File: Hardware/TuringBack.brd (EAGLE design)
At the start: 107 x 49.5 mm, 45 parts, among them IC11 78L09, IC12 78L09, IC7 TL072P

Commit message: Rev 4 Front and Back Boards complete
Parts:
- renumbered BACK_BUS2 to LINK1, BACK_PWR to LINK2, BUS_1_BACK to LINK3
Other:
- board text added: ">>RED>>"
- board text added: "EXPANDER OUTPUTS ONLY"
- board text added: "Music Thing Modular Turing Machine Rev4 Back Board Designed in Herne Hill, London By Tom Whitwell January 2016 CC-BY-SA musicthing.co.uk"
- board text removed: "Music Thing Modular Turing Machine Rev4 Prototype 1 Back Board Designed in Herne Hill, London By Tom Whitwell September 2015 CC-BY-SA"

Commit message: Finalised V4 PCBs
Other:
- board text added: "Allen Strange"
- board text added: "Cage"
- board text added: "Dieter Doepfer"
- board text added: "Don Buchla"
- board text added: "Fredkin & Minsky"
- board text added: "Grant Richter"
- board text added: "Hal Chamberlin"
- board text added: "Inspired by:"
- board text added: "John"
- board text added: "K.F.W"
- board text added: "Ken Stone"
- board text added: "Lunetta"
- board text added: "Navs"
- board text added: "Nicholas Collins"
- board text added: "Philip Glass"
- board text added: "Stanley"
- board text added: "Steve Reich"
- board text added: "Steven Grimley-Taylor"
- board text added: "Terry Riley"
- board text added: "The Muff Wigglers"
- board text added: "Tony Steventon"
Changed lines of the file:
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@@
 <layer number="14" name="Route14" color="1" fill="6" visible="no" active="no"/>
 <layer number="15" name="Route15" color="4" fill="6" visible="no" active="yes"/>
-<layer number="16" name="Bottom" color="1" fill="1" visible="no" active="yes"/>
+<layer number="16" name="Bottom" color="1" fill="1" visible="yes" active="yes"/>
 <layer number="17" name="Pads" color="10" fill="1" visible="yes" active="yes"/>
 <layer number="18" name="Vias" color="2" fill="1" visible="yes" active="yes"/>
-<layer number="19" name="Unrouted" color="6" fill="1" visible="no" active="yes"/>
+<layer number="19" name="Unrouted" color="6" fill="1" visible="yes" active="yes"/>
 <layer number="20" name="Dimension" color="15" fill="1" visible="yes" active="yes"/>
-<layer number="21" name="tPlace" color="7" fill="1" visible="yes" active="yes"/>
-<layer number="22" name="bPlace" color="7" fill="1" visible="no" active="yes"/>
-<layer number="23" name="tOrigins" color="15" fill="1" visible="yes" active="yes"/>
-<layer number="24" name="bOrigins" color="15" fill="1" visible="no" active="yes"/>
-<layer number="25" name="tNames" color="7" fill="1" visible="yes" active="yes"/>
+<layer number="21" name="tPlace" color="7" fill="1" visible="no" active="yes"/>
+<layer number="22" name="bPlace" color="7" fill="1" visible="yes" active="yes"/>
+<layer number="23" name="tOrigins" color="15" fill="1" visible="no" active="yes"/>
+<layer number="24" name="bOrigins" color="15" fill="1" visible="yes" active="yes"/>
+<layer number="25" name="tNames" color="7" fill="1" visible="no" active="yes"/>
 <layer number="26" name="bNames" color="7" fill="1" visible="no" active="yes"/>
-<layer number="27" name="tValues" color="7" fill="1" visible="yes" active="yes"/>
+<layer number="27" name="tValues" color="7" fill="1" visible="no" active="yes"/>
 <layer number="28" name="bValues" color="7" fill="1" visible="no" active="yes"/>
 <layer number="29" name="tStop" color="7" fill="3" visible="no" active="yes"/>
-<layer number="30" name="bStop" color="7" fill="6" visible="no" active="yes"/>
+<layer number="30" name="bStop" color="7" fill="6" visible="yes" active="yes"/>
 <layer number="31" name="tCream" color="7" fill="4" visible="no" active="yes"/>
 <layer number="32" name="bCream" color="7" fill="5" visible="no" active="yes"/>
@@
 <layer number="40" name="bKeepout" color="1" fill="11" visible="no" active="yes"/>
 <layer number="41" name="tRestrict" color="4" fill="10" visible="no" active="yes"/>
-<layer number="42" name="bRestrict" color="1" fill="10" visible="no" active="yes"/>
+<layer number="42" name="bRestrict" color="1" fill="10" visible="yes" active="yes"/>
 <layer number="43" name="vRestrict" color="2" fill="10" visible="no" active="yes"/>
 <layer number="44" name="Drills" color="7" fill="1" visible="no" active="yes"/>
@@
 <wire x1="107" y1="49.5" x2="0" y2="49.5" width="0" layer="20"/>
 <wire x1="-15.875" y1="24.75" x2="121.285" y2="24.75" width="0.05" layer="51"/>
-<text x="98.425" y="1.27" size="1.016" layer="22" font="vector" rot="SMR90">Music Thing Modular Turing Machine
+<text x="84.455" y="27.305" size="1.016" layer="22" font="vector" rot="SMR0">Music Thing Modular Turing Machine
 Rev4  Back Board
 Designed in Herne Hill, London By Tom Whitwell
@@
 </polygon>
 <text x="84.455" y="13.97" size="2.286" layer="22" rot="MR0">EXPANDER OUTPUTS ONLY</text>
+<text x="104.127234375" y="27.377475" size="1.016" layer="30" ratio="12" rot="MR90">Don Buchla</text>
+<text x="98.627628125" y="31.972203125" size="1.016" layer="30" ratio="12" rot="MR90">Ken Stone</text>
+<text x="100.630615625" y="27.0115" size="1.016" layer="30" ratio="12" rot="MR90">Grant Richter</text>
+<text x="105.605978125" y="18.229196875" size="1.016" layer="30" ratio="12" rot="MR90">Hal Chamberlin</text>
+<text x="102.2196125" y="21.173090625" size="1.016" layer="30" ratio="12" rot="MR90">Allen Strange</text>
+<text x="94.02604375" y="33.508940625" size="1.016" layer="30" ratio="12" rot="MR90">Fredkin &amp; Minsky</text>
+<text x="96.389121875" y="35.142478125" size="1.016" layer="30" ratio="12" rot="MR90">Nicholas Collins</text>
+<text x="98.4197375" y="10.113390625" size="1.016" layer="30" ratio="12" rot="MR90">Navs</text>
+<text x="90.79385" y="42.12758125" size="1.016" layer="30" ratio="12" rot="MR90">Lunetta</text>
+<text x="99.34384375" y="15.06238125" size="1.016" layer="30" ratio="12" rot="MR90">Dieter Doepfer</text>
+<text x="105.269009375" y="36.180021875" size="1.016" layer="30" ratio="12" rot="MR90">Philip Glass</text>
+<text x="103.112259375" y="38.498478125" size="1.016" layer="30" ratio="12" rot="MR90">Steve Reich</text>
+<text x="103.34131875" y="1.8847875" size="1.016" layer="30" ratio="12" rot="MR90">Steven Grimley-Taylor</text>
+<text x="92.112265625" y="39.271515625" size="1.016" layer="30" ratio="12" rot="MR90">Stanley</text>
+<text x="101.038353125" y="5.615478125" size="1.016" layer="30" ratio="12" rot="MR90">The Muff Wigglers</text>
+<text x="96.4004875" y="14.234275" size="1.016" layer="30" ratio="12" rot="MR90">K.F.W</text>
+<text x="101.271" y="39.003278125" size="1.016" layer="30" ratio="12" rot="MR90">John</text>
+<text x="100.1762625" y="39.752578125" size="1.016" layer="30" ratio="12" rot="MR90">Cage</text>
+<text x="99.302259375" y="44.213478125" size="1.016" layer="30" ratio="12" rot="MR90">Terry
+Riley</text>
+<text x="105.605978125" y="2.354196875" size="1.016" layer="30" ratio="12" rot="MR90">Inspired by:</text>
+<text x="94.4954875" y="9.154275" size="1.016" layer="30" ratio="12" rot="MR90">Tony
+Steventon</text>
 </plain>
 <attributes>

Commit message: Silkscreen change on Back Board
Added + - symbols to fuses in power supply
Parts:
- +FUSE: value FUSE -> +FUSE
- -FUSE: value FUSE -> -FUSE
- renumbered F1 to +FUSE, F2 to -FUSE
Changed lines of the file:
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@@
 <layer number="19" name="Unrouted" color="6" fill="1" visible="yes" active="yes"/>
 <layer number="20" name="Dimension" color="15" fill="1" visible="yes" active="yes"/>
-<layer number="21" name="tPlace" color="7" fill="1" visible="no" active="yes"/>
-<layer number="22" name="bPlace" color="7" fill="1" visible="yes" active="yes"/>
-<layer number="23" name="tOrigins" color="15" fill="1" visible="no" active="yes"/>
-<layer number="24" name="bOrigins" color="15" fill="1" visible="yes" active="yes"/>
-<layer number="25" name="tNames" color="7" fill="1" visible="no" active="yes"/>
+<layer number="21" name="tPlace" color="7" fill="1" visible="yes" active="yes"/>
+<layer number="22" name="bPlace" color="7" fill="1" visible="no" active="yes"/>
+<layer number="23" name="tOrigins" color="15" fill="1" visible="yes" active="yes"/>
+<layer number="24" name="bOrigins" color="15" fill="1" visible="no" active="yes"/>
+<layer number="25" name="tNames" color="7" fill="1" visible="yes" active="yes"/>
 <layer number="26" name="bNames" color="7" fill="1" visible="no" active="yes"/>
-<layer number="27" name="tValues" color="7" fill="1" visible="no" active="yes"/>
+<layer number="27" name="tValues" color="7" fill="1" visible="yes" active="yes"/>
 <layer number="28" name="bValues" color="7" fill="1" visible="no" active="yes"/>
 <layer number="29" name="tStop" color="7" fill="3" visible="no" active="yes"/>
@@
 <attribute name="VALUE" x="12.192" y="1.524" size="1.016" layer="27" ratio="10" rot="R180"/>
 </element>
-<element name="F1" library="TomW" package="C050H075X075" value="FUSE" x="6.35" y="15.875" smashed="yes">
-<attribute name="VALUE" x="5.08" y="15.875" size="0.889" layer="27" ratio="10"/>
+<element name="+FUSE" library="TomW" package="C050H075X075" value="+FUSE" x="6.35" y="15.875" smashed="yes">
+<attribute name="VALUE" x="4.445" y="15.875" size="0.889" layer="27" ratio="10"/>
 </element>
-<element name="F2" library="TomW" package="C050H075X075" value="FUSE" x="6.35" y="5.715" smashed="yes">
-<attribute name="VALUE" x="5.08" y="5.715" size="0.889" layer="27" ratio="10"/>
+<element name="-FUSE" library="TomW" package="C050H075X075" value="-FUSE" x="6.35" y="5.715" smashed="yes">
+<attribute name="VALUE" x="4.572" y="5.715" size="0.889" layer="27" ratio="10"/>
 </element>
 <element name="L1" library="inductors" package="BL01RN1A" value="BL01RN1A" x="17.78" y="17.78" smashed="yes" rot="R20"/>
@@
 <contactref element="SV1" pad="10"/>
 <contactref element="SV1" pad="9"/>
-<contactref element="F1" pad="1"/>
+<contactref element="+FUSE" pad="1"/>
 <contactref element="D5" pad="C"/>
 <wire x1="13.97" y1="9.525" x2="13.97" y2="12.065" width="0.8128" layer="1"/>
@@
 <contactref element="SV1" pad="1"/>
 <contactref element="SV1" pad="2"/>
-<contactref element="F2" pad="1"/>
+<contactref element="-FUSE" pad="1"/>
 <contactref element="D6" pad="A"/>
 <wire x1="3.81" y1="12.065" x2="3.81" y2="9.525" width="0.8128" layer="1"/>
@@
 <signal name="N$42" class="1">
 <contactref element="L1" pad="1"/>
-<contactref element="F1" pad="2"/>
+<contactref element="+FUSE" pad="2"/>
 <wire x1="8.89" y1="15.875" x2="12.838821875" y2="15.875" width="0.8128" layer="1"/>
 <wire x1="12.838821875" y1="15.875" x2="13.006359375" y2="16.0425375" width="0.8128" layer="1"/>
 </signal>
 <signal name="N$44" class="1">
-<contactref element="F2" pad="2"/>
+<contactref element="-FUSE" pad="2"/>
 <contactref element="L2" pad="1"/>
 <wire x1="8.89" y1="5.715" x2="12.5389" y2="5.715" width="0.8128" layer="1"/>

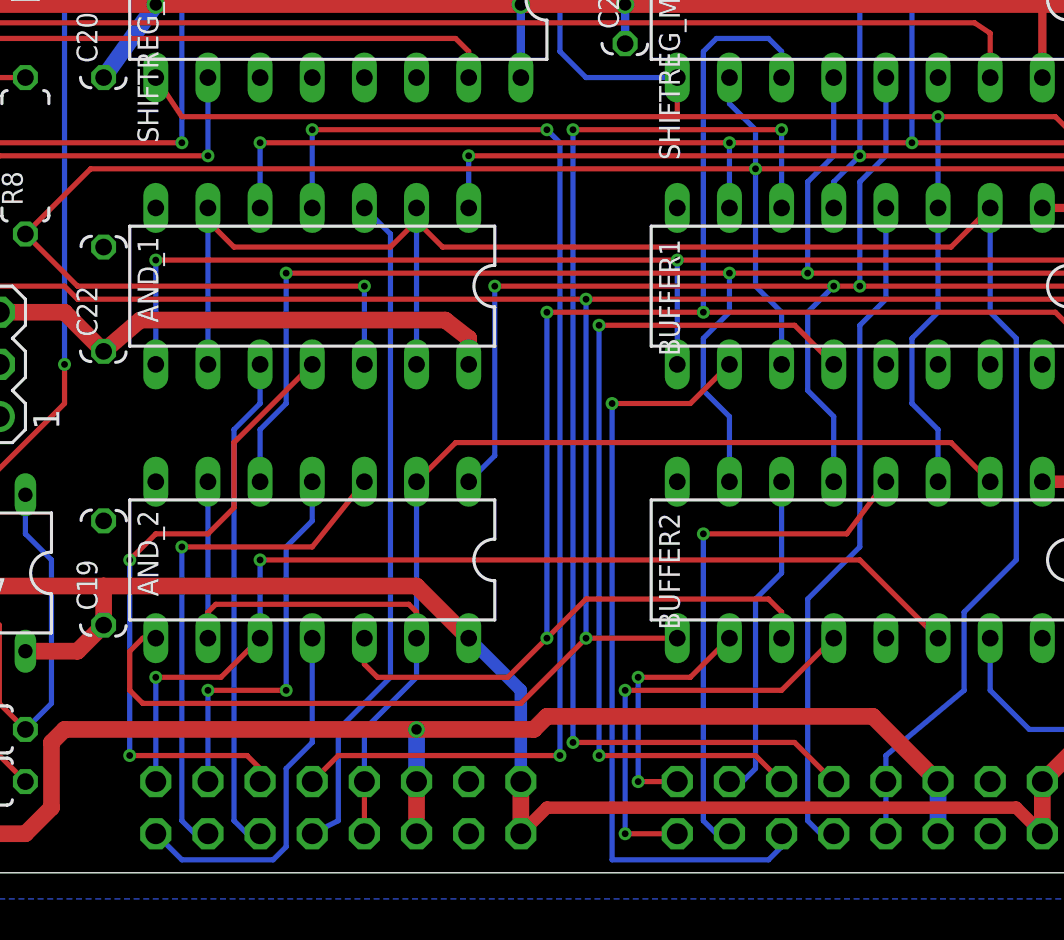
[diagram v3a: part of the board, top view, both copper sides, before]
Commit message: Schematic fixed, back board needs to be routed
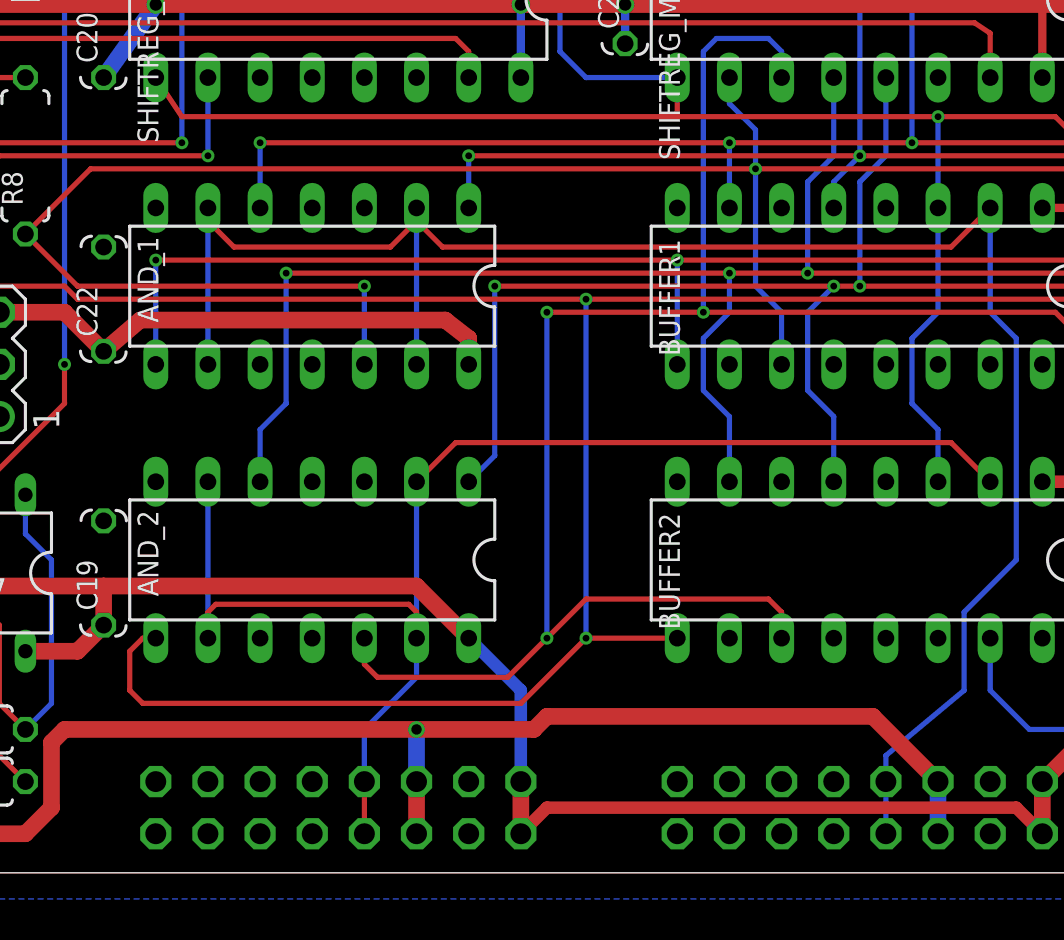
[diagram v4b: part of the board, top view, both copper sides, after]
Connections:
- net GATE1: now also BUFFER1.4; no longer BUFFER2.10
- net GATE2: now also BUFFER1.6; no longer BUFFER2.12
- net GATE3: now also BUFFER1.10; no longer BUFFER2.6
- net GATE4: now also BUFFER1.12; no longer BUFFER2.4
- net GATE5: now also BUFFER2.4; no longer BUFFER1.12
- net GATE6: now also BUFFER2.6; no longer BUFFER1.10
- net GATE7: now also BUFFER2.12; no longer BUFFER1.6
- net GATE8: now also BUFFER2.10; no longer BUFFER1.4
- net PULSE1: now also AND_1.3; no longer AND_2.10
- net PULSE2: now also AND_1.4; no longer AND_2.11
- net PULSE3: now also AND_1.10; no longer AND_2.4
- net PULSE4: now also AND_1.11; no longer AND_2.3
- net PULSE5: now also AND_2.3; no longer AND_1.11
- net PULSE6: now also AND_2.4; no longer AND_1.10
- net PULSE7: now also AND_2.11; no longer AND_1.4
- net PULSE8: now also AND_2.10; no longer AND_1.3
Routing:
- net PULSE7: track 58.6 -> 0.00 mm, vias 3 -> 0
- net GATE7: track 57.3 -> 0.00 mm, vias 3 -> 0
- net PULSE1: track 49.4 -> 0.00 mm, vias 2 -> 0
- net GATE5: track 42.6 -> 0.00 mm, vias 2 -> 0
- net GATE6: track 37.9 -> 0.00 mm, vias 1 -> 0
- net GATE8: track 33.0 -> 0.00 mm
- net PULSE8: track 32.8 -> 0.00 mm
- net PULSE5: track 31.5 -> 0.00 mm, vias 2 -> 0
- net GATE4: track 25.7 -> 0.00 mm, vias 1 -> 0
- net PULSE4: track 25.3 -> 0.00 mm, vias 1 -> 0
- net PULSE6: track 24.3 -> 0.00 mm
- net GATE2: track 20.7 -> 0.00 mm, vias 2 -> 0
- net PULSE3: track 18.9 -> 0.00 mm, vias 2 -> 0
- net PULSE2: track 17.8 -> 0.00 mm
- net GATE3: track 16.0 -> 0.00 mm
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
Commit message: routing started
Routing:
- net GATE2: track 0.00 -> 48.6 mm, vias 0 -> 2
- net GATE1: track 0.00 -> 40.9 mm, vias 0 -> 2
- net GATE4: track 0.00 -> 26.0 mm
- net GATE3: track 0.00 -> 21.4 mm
- net GATE6: track 0.00 -> 18.2 mm, vias 0 -> 1
- net GATE8: track 0.00 -> 17.8 mm
- net GATE7: track 0.00 -> 6.98 mm
- net -12V_BACK: track 105.0 -> 104.3 mm
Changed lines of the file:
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@@
 <contactref element="GATES" pad="1"/>
 <contactref element="BUFFER1" pad="4"/>
-<wire x1="67.31" y1="4.445" x2="77.47" y2="32.385" width="0" layer="19" extent="1-1"/>
+<wire x1="77.47" y1="32.385" x2="77.47" y2="27.94" width="0.254" layer="16"/>
+<wire x1="77.47" y1="27.94" x2="76.2" y2="26.67" width="0.254" layer="16"/>
+<wire x1="76.2" y1="26.67" x2="64.77" y2="26.67" width="0.254" layer="1"/>
+<wire x1="64.77" y1="26.67" x2="64.77" y2="6.985" width="0.254" layer="16"/>
+<wire x1="64.77" y1="6.985" x2="67.31" y2="4.445" width="0.254" layer="16"/>
+<via x="76.2" y="26.67" extent="1-16" drill="0.3302"/>
+<via x="64.77" y="26.67" extent="1-16" drill="0.3302"/>
 </signal>
 <signal name="GATE2">
 <contactref element="GATES" pad="2"/>
 <contactref element="BUFFER1" pad="6"/>
-<wire x1="67.31" y1="1.905" x2="72.39" y2="32.385" width="0" layer="19" extent="1-1"/>
+<wire x1="72.39" y1="32.385" x2="72.39" y2="36.195" width="0.254" layer="16"/>
+<wire x1="72.39" y1="36.195" x2="63.5" y2="36.195" width="0.254" layer="1"/>
+<wire x1="63.5" y1="36.195" x2="63.5" y2="5.715" width="0.254" layer="16"/>
+<wire x1="63.5" y1="5.715" x2="67.31" y2="1.905" width="0.254" layer="16"/>
+<via x="72.39" y="36.195" extent="1-16" drill="0.3302"/>
+<via x="63.5" y="36.195" extent="1-16" drill="0.3302"/>
 </signal>
 <signal name="GATE3">
 <contactref element="GATES" pad="3"/>
 <contactref element="BUFFER1" pad="10"/>
-<wire x1="69.85" y1="4.445" x2="69.85" y2="24.765" width="0" layer="19" extent="1-1"/>
+<wire x1="69.85" y1="24.765" x2="69.85" y2="23.495" width="0.254" layer="16"/>
+<wire x1="69.85" y1="23.495" x2="71.12" y2="22.225" width="0.254" layer="16"/>
+<wire x1="71.12" y1="22.225" x2="71.12" y2="8.89" width="0.254" layer="16"/>
+<wire x1="71.12" y1="8.89" x2="69.85" y2="7.62" width="0.254" layer="16"/>
+<wire x1="69.85" y1="7.62" x2="69.85" y2="4.445" width="0.254" layer="16"/>
 </signal>
 <signal name="GATE4">
 <contactref element="GATES" pad="4"/>
 <contactref element="BUFFER1" pad="12"/>
-<wire x1="69.85" y1="1.905" x2="74.93" y2="24.765" width="0" layer="19" extent="1-1"/>
+<wire x1="69.85" y1="1.905" x2="71.12" y2="3.175" width="0.254" layer="16"/>
+<wire x1="71.12" y1="3.175" x2="71.12" y2="6.985" width="0.254" layer="16"/>
+<wire x1="71.12" y1="6.985" x2="73.66" y2="9.525" width="0.254" layer="16"/>
+<wire x1="73.66" y1="9.525" x2="73.66" y2="14.605" width="0.254" layer="16"/>
+<wire x1="73.66" y1="14.605" x2="76.2" y2="17.145" width="0.254" layer="16"/>
+<wire x1="76.2" y1="17.145" x2="76.2" y2="23.495" width="0.254" layer="16"/>
+<wire x1="76.2" y1="23.495" x2="74.93" y2="24.765" width="0.254" layer="16"/>
 </signal>
 <signal name="GATE5">
@@
 <contactref element="GATES" pad="6"/>
 <contactref element="BUFFER2" pad="6"/>
-<wire x1="72.39" y1="1.905" x2="72.39" y2="19.05" width="0" layer="19" extent="1-1"/>
+<wire x1="72.39" y1="19.05" x2="72.39" y2="15.875" width="0.254" layer="1"/>
+<wire x1="72.39" y1="15.875" x2="73.66" y2="14.605" width="0.254" layer="1"/>
+<wire x1="73.66" y1="14.605" x2="73.66" y2="8.255" width="0.254" layer="1"/>
+<wire x1="73.66" y1="8.255" x2="73.66" y2="3.175" width="0.254" layer="16"/>
+<wire x1="73.66" y1="3.175" x2="72.39" y2="1.905" width="0.254" layer="16"/>
+<via x="73.66" y="8.255" extent="1-16" drill="0.3302"/>
 </signal>
 <signal name="GATE7">
 <contactref element="GATES" pad="7"/>
 <contactref element="BUFFER2" pad="12"/>
-<wire x1="74.93" y1="4.445" x2="74.93" y2="11.43" width="0" layer="19" extent="1-1"/>
+<wire x1="74.93" y1="4.445" x2="74.93" y2="11.43" width="0.254" layer="16"/>
 </signal>
 <signal name="GATE8">
 <contactref element="GATES" pad="8"/>
 <contactref element="BUFFER2" pad="10"/>
-<wire x1="74.93" y1="1.905" x2="69.85" y2="11.43" width="0" layer="19" extent="1-1"/>
+<wire x1="69.85" y1="11.43" x2="69.85" y2="9.525" width="0.254" layer="16"/>
+<wire x1="69.85" y1="9.525" x2="68.58" y2="8.255" width="0.254" layer="16"/>
+<wire x1="68.58" y1="8.255" x2="68.58" y2="1.27" width="0.254" layer="16"/>
+<wire x1="68.58" y1="1.27" x2="69.215" y2="0.635" width="0.254" layer="16"/>
+<wire x1="69.215" y1="0.635" x2="73.66" y2="0.635" width="0.254" layer="16"/>
+<wire x1="73.66" y1="0.635" x2="74.93" y2="1.905" width="0.254" layer="16"/>
 </signal>
 <signal name="+9V_1" class="1">
@@
 <wire x1="22.5536375" y1="2.7075375" x2="22.5536375" y2="8.5613625" width="0.8128" layer="1"/>
 <wire x1="80.01" y1="1.905" x2="80.01" y2="4.445" width="0.8128" layer="16"/>
-<wire x1="80.01" y1="4.445" x2="76.835" y2="7.62" width="0.8128" layer="1"/>
-<wire x1="76.835" y1="7.62" x2="60.96" y2="7.62" width="0.8128" layer="1"/>
-<wire x1="60.96" y1="7.62" x2="60.325" y2="6.985" width="0.8128" layer="1"/>
-<wire x1="60.325" y1="6.985" x2="54.61" y2="6.985" width="0.8128" layer="1"/>
+<wire x1="80.01" y1="4.445" x2="76.835" y2="6.985" width="0.8128" layer="1"/>
+<wire x1="76.835" y1="6.985" x2="54.61" y2="6.985" width="0.8128" layer="1"/>
 <wire x1="54.61" y1="6.985" x2="54.61" y2="4.445" width="0.8128" layer="16"/>
 <wire x1="54.61" y1="4.445" x2="54.61" y2="1.905" width="0.8128" layer="1"/>

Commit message: First fully routed
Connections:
- net B1_BACK: now also AND_2.1; no longer AND_2.8
- net B4_BACK: now also AND_2.8; no longer AND_2.1
- net PULSE5: now also AND_2.10; no longer AND_2.3
- net PULSE8: now also AND_2.3; no longer AND_2.10
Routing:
- net PULSE1: track 0.00 -> 71.8 mm, vias 0 -> 2
- net PULSE2: track 0.00 -> 39.8 mm, vias 0 -> 1
- net B1_BACK: track 167.3 -> 135.6 mm, vias 2 -> 3
- net PULSE4: track 0.00 -> 25.0 mm
- net PULSE3: track 0.00 -> 22.4 mm
- net B6_BACK: track 99.7 -> 77.9 mm
- net B5_BACK: track 103.4 -> 82.4 mm
- net B2_BACK: track 96.1 -> 77.3 mm, vias 3 -> 2
- net PULSE6: track 0.00 -> 18.2 mm
- net PULSE8: track 0.00 -> 18.2 mm
- net GATE4: track 26.0 -> 43.8 mm, vias 0 -> 2
- net GATE5: track 0.00 -> 16.7 mm
- net CLOCK_BACK: track 117.5 -> 101.7 mm, vias 1 -> 4
- net B4_BACK: track 69.5 -> 84.9 mm
- net PULSE_OUT_BACK: track 36.5 -> 27.6 mm, vias 0 -> 1
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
